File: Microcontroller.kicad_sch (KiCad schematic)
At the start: 1 part, among them U1 ATmega328-A

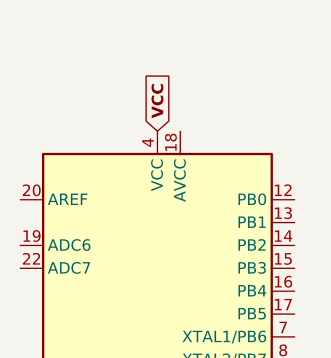
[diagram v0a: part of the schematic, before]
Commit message: Keyboard Data Changes and added footprints
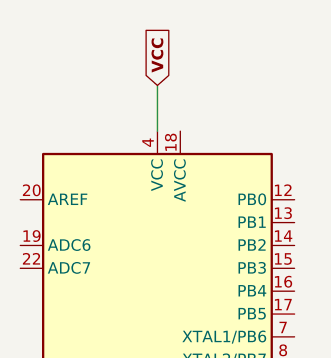
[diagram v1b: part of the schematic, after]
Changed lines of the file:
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@@
 	(generator_version "8.0")
 	(paper "A4")
+	(wire
+		(pts
+			(xy 100.33 62.23) (xy 100.33 67.31)
+		)
+		(stroke
+			(width 0)
+			(type default)
+		)
+	)
 	(global_label "VCC"
 		(shape input)
-		(at 100.33 67.31 90)
+		(at 100.33 62.23 90)
 		(fields_autoplaced yes)
 		(effects
@@
 		)
 		(property "Intersheetrefs" "${INTERSHEET_REFS}"
-			(at 100.33 60.2202 90)
+			(at 100.33 55.1402 90)
 			(effects
 				(font

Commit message: Atmega34u4
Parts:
- removed U1: ATmega328-A, Package_QFP:TQFP-32_7x7mm_P0.8mm, symbol MCU_Microchip_ATmega:ATmega328-A
- added U1: ATmega32U4-A, Package_QFP:TQFP-44_10x10mm_P0.8mm, symbol MCU_Microchip_ATmega:ATmega32U4-A
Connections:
- net VCC: now also U1.14 (VCC), U1.34 (VCC)
- new net: U1.15 (GND), U1.23 (GND), U1.35 (GND), U1.43 (GND)
- new net: U1.24 (AVCC), U1.44 (AVCC)
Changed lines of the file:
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@@
 	)
 	(symbol
-		(lib_id "MCU_Microchip_ATmega:ATmega328-A")
-		(at 100.33 105.41 0)
+		(lib_id "MCU_Microchip_ATmega:ATmega32U4-A")
+		(at 100.33 113.03 0)
 		(unit 1)
 		(exclude_from_sim no)
@@
 		(fields_autoplaced yes)
 		(property "Reference" "U1"
-			(at 102.5241 143.51 0)
+			(at 102.5241 158.75 0)
 			(effects
 				(font
@@
 			)
 		)
-		(property "Value" "ATmega328-A"
-			(at 102.5241 146.05 0)
+		(property "Value" "ATmega32U4-A"
+			(at 102.5241 161.29 0)
 			(effects
 				(font
@@
 			)
 		)
-		(property "Footprint" "Package_QFP:TQFP-32_7x7mm_P0.8mm"
-			(at 100.33 105.41 0)
+		(property "Footprint" "Package_QFP:TQFP-44_10x10mm_P0.8mm"
+			(at 100.33 113.03 0)
 			(effects
 				(font
@@
 			)
 		)
-		(property "Datasheet" "http://ww1.microchip.com/downloads/en/DeviceDoc/ATmega328_P%20AVR%20MCU%20with%20picoPower%20Technology%20Data%20Sheet%2040001984A.pdf"
-			(at 100.33 105.41 0)
+		(property "Datasheet" "http://ww1.microchip.com/downloads/en/DeviceDoc/Atmel-7766-8-bit-AVR-ATmega16U4-32U4_Datasheet.pdf"
+			(at 100.33 113.03 0)
 			(effects
 				(font
@@
 			)
 		)
-		(property "Description" "20MHz, 32kB Flash, 2kB SRAM, 1kB EEPROM, TQFP-32"
-			(at 100.33 105.41 0)
+		(property "Description" "16MHz, 32kB Flash, 2.5kB SRAM, 1kB EEPROM, USB 2.0, TQFP-44"
+			(at 100.33 113.03 0)
 			(effects
 				(font
@@
 			)
 		)
+		(pin "28"
+		)
+		(pin "42"
+		)
+		(pin "31"
+		)
 		(pin "32"
+		)
+		(pin "36"
+		)
+		(pin "41"
+		)
+		(pin "10"
+		)
+		(pin "33"
+		)
+		(pin "30"
+		)
+		(pin "2"
+		)
+		(pin "38"
+		)
+		(pin "40"
+		)
+		(pin "5"
+		)
+		(pin "6"
+		)
+		(pin "20"
+		)
+		(pin "44"
+		)
+		(pin "7"
+		)
+		(pin "22"
+		)
+		(pin "37"
+		)
+		(pin "23"
+		)
+		(pin "24"
+		)
+		(pin "35"
+		)
+		(pin "26"
+		)
+		(pin "34"
+		)
+		(pin "4"
+		)
+		(pin "12"
+		)
+		(pin "43"
 		)
 		(pin "9"
 		)
+		(pin "13"
+		)
+		(pin "29"
+		)
+		(pin "39"
+		)
+		(pin "21"
+		)
+		(pin "25"
+		)
+		(pin "17"
+		)
+		(pin "18"
+		)
 		(pin "15"
-		)
-		(pin "20"
-		)
-		(pin "6"
 		)
 		(pin "19"
 		)
-		(pin "30"
+		(pin "1"
 		)
-		(pin "4"
+		(pin "11"
 		)
-		(pin "5"
+		(pin "3"
+		)
+		(pin "27"
+		)
+		(pin "8"
+		)
+		(pin "14"
 		)
 		(pin "16"
 		)
-		(pin "18"
-		)
-		(pin "24"
-		)
-		(pin "11"
-		)
-		(pin "12"
-		)
-		(pin "10"
-		)
-		(pin "21"
-		)
-		(pin "14"
-		)
-		(pin "13"
-		)
-		(pin "23"
-		)
-		(pin "2"
-		)
-		(pin "7"
-		)
-		(pin "31"
-		)
-		(pin "1"
-		)
-		(pin "27"
-		)
-		(pin "17"
-		)
-		(pin "3"
-		)
-		(pin "22"
-		)
-		(pin "25"
-		)
-		(pin "28"
-		)
-		(pin "8"
-		)
-		(pin "29"
-		)
-		(pin "26"
-		)
 		(instances
-			(project "EEProject"
+			(project ""
 				(path "/3aa1ef99-b297-42d2-a07b-7cd664ecf53c/681e2464-01d4-4174-9887-b09f82d30530"
 					(reference "U1")

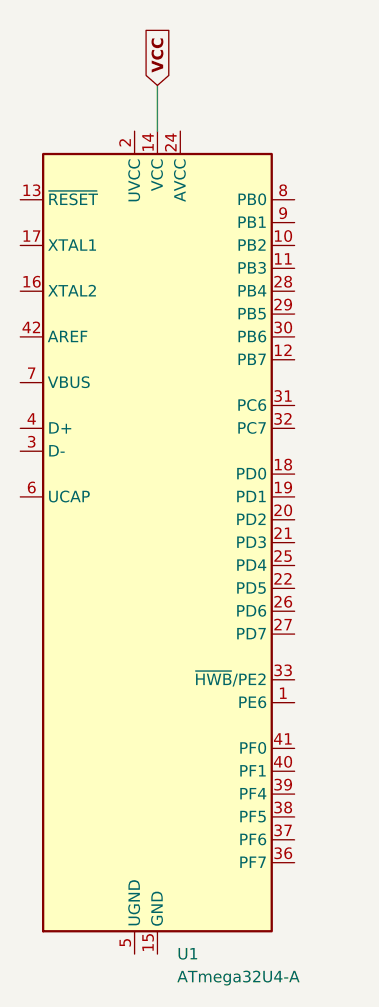
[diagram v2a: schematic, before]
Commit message: UART passive components
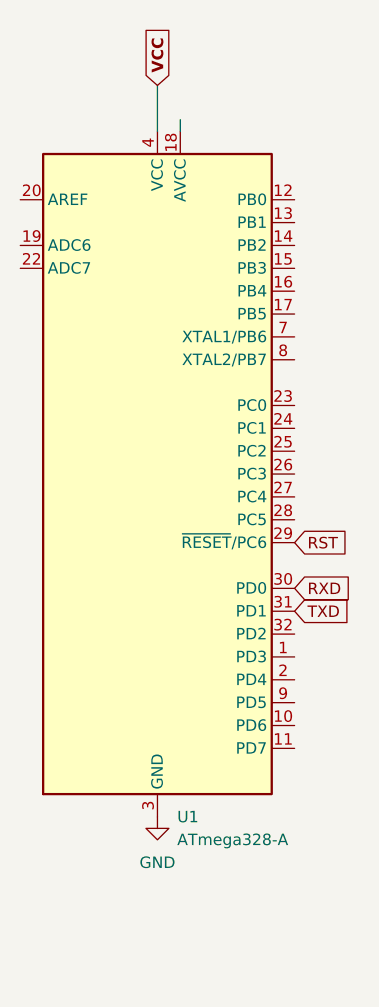
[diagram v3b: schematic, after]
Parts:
- removed U1: ATmega32U4-A, Package_QFP:TQFP-44_10x10mm_P0.8mm, symbol MCU_Microchip_ATmega:ATmega32U4-A
- added U1: ATmega328-A, Package_QFP:TQFP-32_7x7mm_P0.8mm, symbol MCU_Microchip_ATmega:ATmega328-A
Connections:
- net VCC: now also U1.4 (VCC), U1.6 (VCC)
- new net GND: U1.21 (GND), U1.3 (GND), U1.5 (GND)
- new net RST: U1.29 (~{RESET}/PC6)
- new net RXD: U1.30 (PD0)
- new net TXD: U1.31 (PD1)
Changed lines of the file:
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@@
+	(wire
+		(pts
+			(xy 102.87 66.04) (xy 102.87 67.31)
+		)
+		(stroke
+			(width 0)
+			(type default)
+		)
+	)
 	(wire
 		(pts
@@
 		)
 	)
+	(global_label "RST"
+		(shape input)
+		(at 115.57 113.03 0)
+		(fields_autoplaced yes)
+		(effects
+			(font
+				(size 1.27 1.27)
+			)
+			(justify left)
+		)
+		(property "Intersheetrefs" "${INTERSHEET_REFS}"
+			(at 122.0023 113.03 0)
+			(effects
+				(font
+					(size 1.27 1.27)
+				)
+				(justify left)
+				(hide yes)
+			)
+		)
+	)
+	(global_label "RXD"
+		(shape input)
+		(at 115.57 118.11 0)
+		(fields_autoplaced yes)
+		(effects
+			(font
+				(size 1.27 1.27)
+			)
+			(justify left)
+		)
+		(property "Intersheetrefs" "${INTERSHEET_REFS}"
+			(at 122.3047 118.11 0)
+			(effects
+				(font
+					(size 1.27 1.27)
+				)
+				(justify left)
+				(hide yes)
+			)
+		)
+	)
+	(global_label "TXD"
+		(shape input)
+		(at 115.57 120.65 0)
+		(fields_autoplaced yes)
+		(effects
+			(font
+				(size 1.27 1.27)
+			)
+			(justify left)
+		)
+		(property "Intersheetrefs" "${INTERSHEET_REFS}"
+			(at 122.0023 120.65 0)
+			(effects
+				(font
+					(size 1.27 1.27)
+				)
+				(justify left)
+				(hide yes)
+			)
+		)
+	)
 	(global_label "VCC"
 		(shape input)
@@
 	)
 	(symbol
-		(lib_id "MCU_Microchip_ATmega:ATmega32U4-A")
-		(at 100.33 113.03 0)
+		(lib_id "MCU_Microchip_ATmega:ATmega328-A")
+		(at 100.33 105.41 0)
 		(unit 1)
 		(exclude_from_sim no)
@@
 		(fields_autoplaced yes)
 		(property "Reference" "U1"
-			(at 102.5241 158.75 0)
-			(effects
-				(font
-					(size 1.27 1.27)
-				)
-				(justify left)
-			)
-		)
-		(property "Value" "ATmega32U4-A"
-			(at 102.5241 161.29 0)
-			(effects
-				(font
-					(size 1.27 1.27)
-				)
-				(justify left)
-			)
-		)
-		(property "Footprint" "Package_QFP:TQFP-44_10x10mm_P0.8mm"
-			(at 100.33 113.03 0)
+			(at 102.5241 143.51 0)
+			(effects
+				(font
+					(size 1.27 1.27)
+				)
+				(justify left)
+			)
+		)
+		(property "Value" "ATmega328-A"
+			(at 102.5241 146.05 0)
+			(effects
+				(font
+					(size 1.27 1.27)
+				)
+				(justify left)
+			)
+		)
+		(property "Footprint" "Package_QFP:TQFP-32_7x7mm_P0.8mm"
+			(at 100.33 105.41 0)
 			(effects
 				(font
@@
 			)
 		)
-		(property "Datasheet" "http://ww1.microchip.com/downloads/en/DeviceDoc/Atmel-7766-8-bit-AVR-ATmega16U4-32U4_Datasheet.pdf"
-			(at 100.33 113.03 0)
-			(effects
-				(font
-					(size 1.27 1.27)
-				)
-				(hide yes)
-			)
-		)
-		(property "Description" "16MHz, 32kB Flash, 2.5kB SRAM, 1kB EEPROM, USB 2.0, TQFP-44"
-			(at 100.33 113.03 0)
-			(effects
-				(font
-					(size 1.27 1.27)
-				)
-				(hide yes)
-			)
+		(property "Datasheet" "http://ww1.microchip.com/downloads/en/DeviceDoc/ATmega328_P%20AVR%20MCU%20with%20picoPower%20Technology%20Data%20Sheet%2040001984A.pdf"
+			(at 100.33 105.41 0)
+			(effects
+				(font
+					(size 1.27 1.27)
+				)
+				(hide yes)
+			)
+		)
+		(property "Description" "20MHz, 32kB Flash, 2kB SRAM, 1kB EEPROM, TQFP-32"
+			(at 100.33 105.41 0)
+			(effects
+				(font
+					(size 1.27 1.27)
+				)
+				(hide yes)
+			)
+		)
+		(pin "15"
 		)
 		(pin "28"
 		)
-		(pin "42"
+		(pin "32"
+		)
+		(pin "25"
+		)
+		(pin "2"
+		)
+		(pin "8"
+		)
+		(pin "30"
+		)
+		(pin "12"
+		)
+		(pin "22"
+		)
+		(pin "13"
+		)
+		(pin "27"
+		)
+		(pin "5"
+		)
+		(pin "18"
+		)
+		(pin "21"
+		)
+		(pin "11"
 		)
 		(pin "31"
 		)
-		(pin "32"
-		)
-		(pin "36"
-		)
-		(pin "41"
+		(pin "29"
+		)
+		(pin "17"
+		)
+		(pin "24"
 		)
 		(pin "10"
 		)
-		(pin "33"
-		)
-		(pin "30"
-		)
-		(pin "2"
-		)
-		(pin "38"
-		)
-		(pin "40"
-		)
-		(pin "5"
+		(pin "23"
+		)
+		(pin "26"
+		)
+		(pin "4"
+		)
+		(pin "3"
+		)
+		(pin "14"
+		)
+		(pin "1"
+		)
+		(pin "7"
+		)
+		(pin "20"
 		)
 		(pin "6"
 		)
-		(pin "20"
-		)
-		(pin "44"
-		)
-		(pin "7"
-		)
-		(pin "22"
-		)
-		(pin "37"
-		)
-		(pin "23"
-		)
-		(pin "24"
-		)
-		(pin "35"
-		)
-		(pin "26"
-		)
-		(pin "34"
-		)
-		(pin "4"
-		)
-		(pin "12"
-		)
-		(pin "43"
-		)
 		(pin "9"
 		)
-		(pin "13"
-		)
-		(pin "29"
-		)
-		(pin "39"
-		)
-		(pin "21"
-		)
-		(pin "25"
-		)
-		(pin "17"
-		)
-		(pin "18"
-		)
-		(pin "15"
+		(pin "16"
 		)
 		(pin "19"
-		)
-		(pin "1"
-		)
-		(pin "11"
-		)
-		(pin "3"
-		)
-		(pin "27"
-		)
-		(pin "8"
-		)
-		(pin "14"
-		)
-		(pin "16"
 		)
 		(instances
@@
 					(unit 1)
 				)
+			)
+		)
+	)
+	(symbol
+		(lib_id "power:GND")
+		(at 100.33 143.51 0)
+		(unit 1)
+		(exclude_from_sim no)
+		(in_bom yes)
+		(on_board yes)
+		(dnp no)
+		(fields_autoplaced yes)
+		(property "Reference" "#PWR011"
+			(at 100.33 149.86 0)
+			(effects
+				(font
+					(size 1.27 1.27)
+				)
+				(hide yes)
+			)
+		)
+		(property "Value" "GND"
+			(at 100.33 148.59 0)
+			(effects
+				(font
+					(size 1.27 1.27)
+				)
+			)
+		)
+		(property "Footprint" ""
+			(at 100.33 143.51 0)
+			(effects
+				(font
+					(size 1.27 1.27)
+				)
+				(hide yes)
+			)
+		)
+		(property "Datasheet" ""
+			(at 100.33 143.51 0)
+			(effects
+				(font
+					(size 1.27 1.27)
+				)
+				(hide yes)
+			)
+		)
+		(property "Description" "Power symbol creates a global label with name \"GND\" , ground"
+			(at 100.33 143.51 0)
+			(effects
+				(font
+					(size 1.27 1.27)
+				)
+				(hide yes)
+			)
+		)
+		(pin "1"
+		)
+		(instances
+			(project ""
+				(path "/3aa1ef99-b297-42d2-a07b-7cd664ecf53c/681e2464-01d4-4174-9887-b09f82d30530"
+					(reference "#PWR011")
+					(unit 1)
+				)

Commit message: 11.10.2024
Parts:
- added C6: 0.1u, symbol Device:C
- added C7, C8: 22p, symbol Device:C
- added Y1: 16M, symbol Device:Crystal
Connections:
- net GND: now also C6.2, C7.1, C8.1
- net VCC: now also C6.1
- net XTAL1: now reaches U1.7 (XTAL1/PB6)
- net XTAL1: now also C7.2, Y1.1
- net XTAL2: now reaches U1.8 (XTAL2/PB7)
- net XTAL2: now also C8.2, Y1.2
- net RST renamed RTS
